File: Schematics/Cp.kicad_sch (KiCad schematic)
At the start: 56 parts, among them Q10 J201, Q11 J201, Q3 2SC1815, Q5 2SC1815, Q6 2SC1815, Q7 2SC1815, Q8 2SC1815, Q9 2SC1815, SW1 SW_DPDT_x2, U1 CA3080

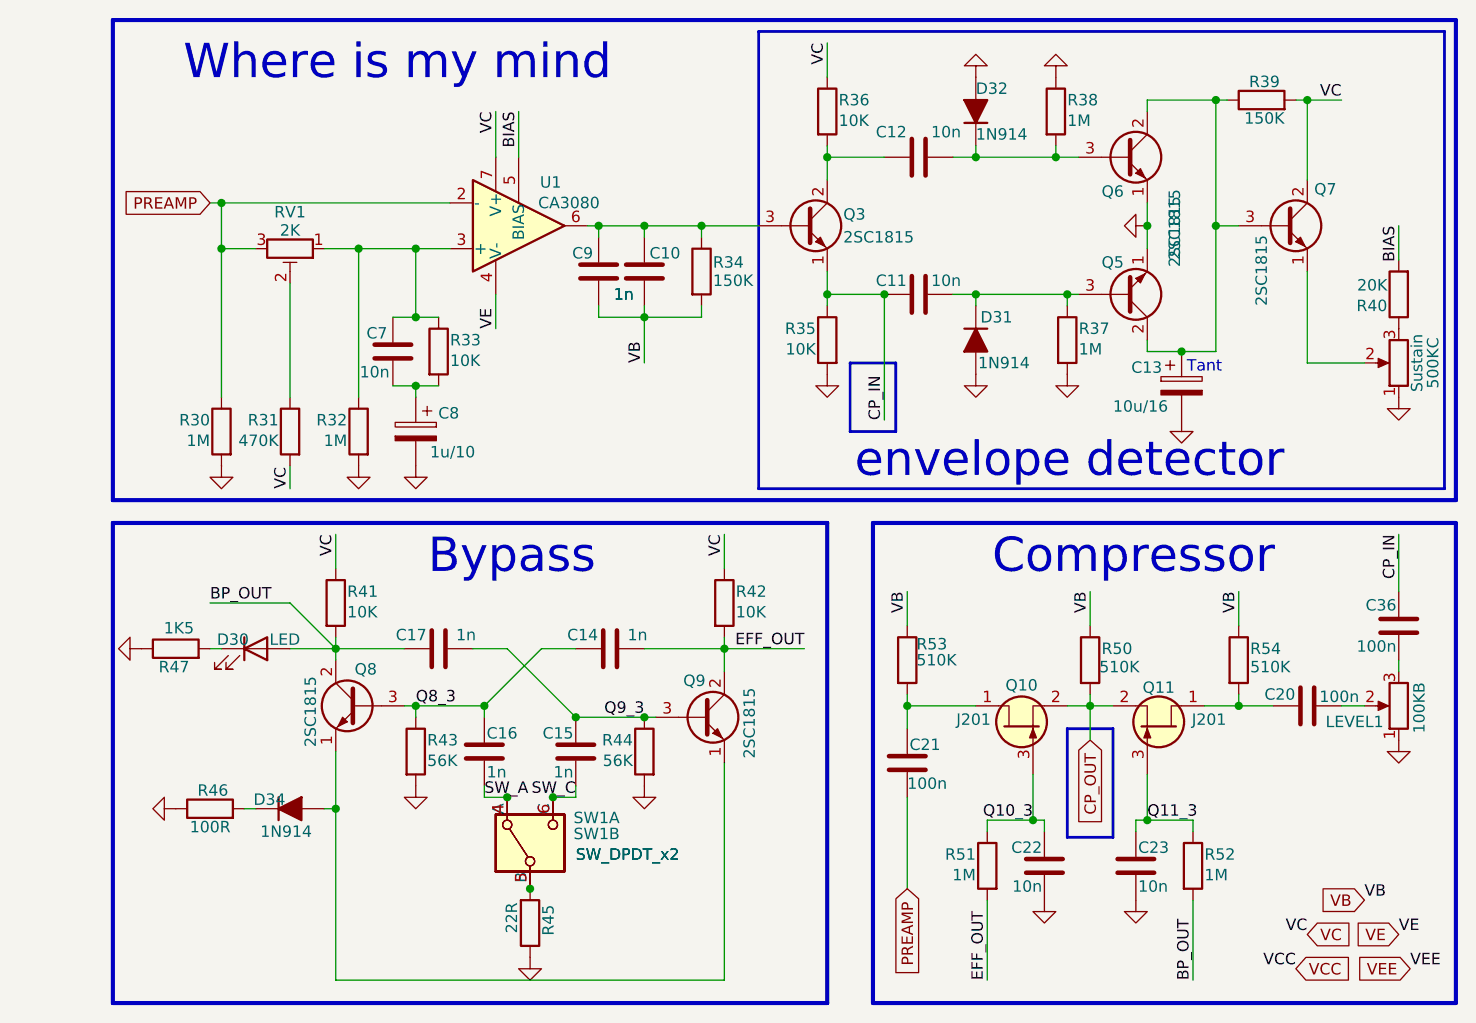
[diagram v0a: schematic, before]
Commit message: Schematic upd
Revorked bypass module, Annotated capacitors, Replaced 2N5484 and j209 with 2SK30A
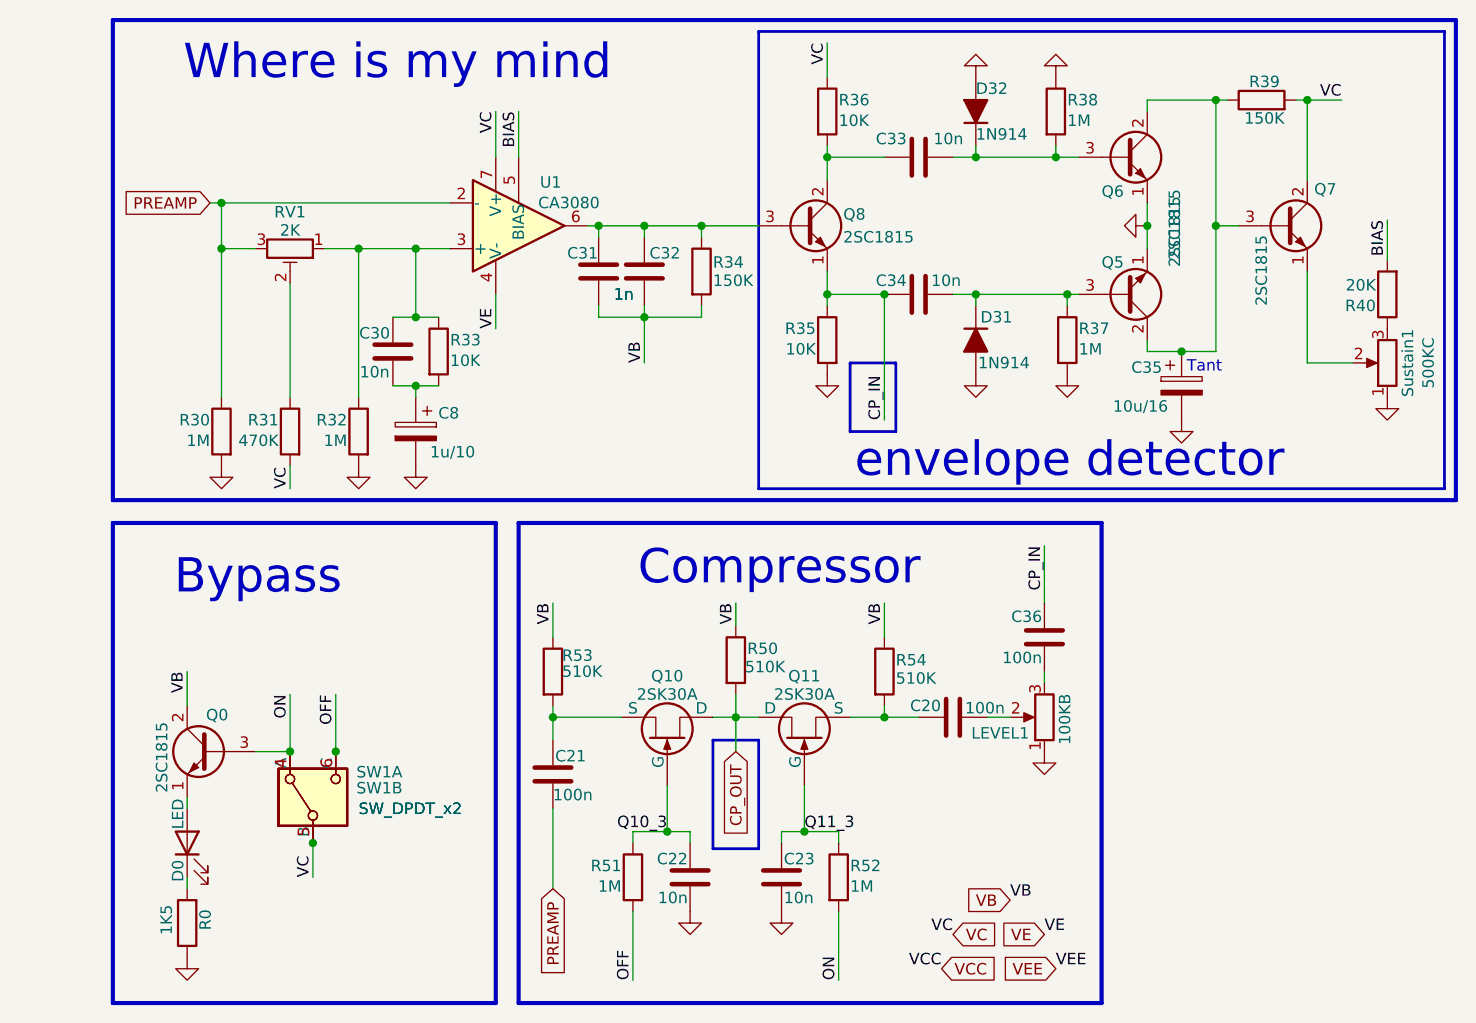
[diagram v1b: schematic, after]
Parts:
- removed C14, C15, C16, C17: 1n, PrLib:C_Disc_D4.3_W1.9_P5.00, symbol Device:C
- removed D30: LED, LED_THT:LED_D3.0mm_Horizontal_O6.35mm_Z6.0mm, symbol Device:LED
- removed D34: 1N914, Diode_THT:D_DO-35_SOD27_P7.62mm_Horizontal, symbol PCM_Diode_AKL:1N914
- removed Q10, Q11: J201, Package_TO_SOT_THT:TO-92_Inline, symbol PCM_Transistor_JFET_AKL:J201
- removed Q9: 2SC1815, Package_TO_SOT_THT:TO-92_Inline, symbol Transistor_BJT:2SC1815
- removed R41, R42: 10K, Resistor_THT:R_Axial_DIN0207_L6.3mm_D2.5mm_P10.16mm_Horizontal, symbol Device:R
- removed R43, R44: 56K, Resistor_THT:R_Axial_DIN0207_L6.3mm_D2.5mm_P10.16mm_Horizontal, symbol Device:R
- removed R45: 22R, Resistor_THT:R_Axial_DIN0207_L6.3mm_D2.5mm_P10.16mm_Horizontal, symbol Device:R
- removed R46: 100R, Resistor_THT:R_Axial_DIN0207_L6.3mm_D2.5mm_P10.16mm_Horizontal, symbol Device:R
- added D0: LED, LED_THT:LED_D3.0mm_Horizontal_O6.35mm_Z6.0mm, symbol Device:LED
- added Q10, Q11: 2SK30A, Package_TO_SOT_THT:TO-92_Inline_Wide, symbol Device:Q_NJFET_DGS
- renumbered C7 to C30, C9 to C31, C10 to C32, C12 to C33, C11 to C34, C13 to C35, Q8 to Q0, Q3 to Q8, R47 to R0, Sustain to Sustain1
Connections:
- net Q8_3 is gone; now on net ON: Q0.3 (B)
- net SW_A is gone; now on net ON: SW1.1 (A), SW1.4 (A)
- net SW_C is gone; now on net OFF: SW1.3 (C), SW1.6 (C)
- net CP_OUT: now also Q10.1 (D), Q11.1 (D)
- net Q10_3: now also Q10.2 (G)
- net Q11_3: now also Q11.2 (G)
- net VB: now also Q0.2 (C)
- net VC: now also SW1.2 (B), SW1.5 (B)
- net at C20.1, R54.2: now also Q11.3 (S)
- net at Q0.1 (E): now also D0.2 (A)
- net at C21.2, R53.2: now also Q10.3 (S)
- net at R0.2: now also D0.1 (K)
- net BP_OUT renamed ON
- net ON: no longer Q0.2 (C)
- net EFF_OUT renamed OFF
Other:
- moved on the sheet: C20, C21, C22, C23, C36, LEVEL1, Q0, R0, R40, R50, R51, R52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

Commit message: Schematic upd
Revorked mix module, Bypass upd, Replaced 1N914 with 1N4148
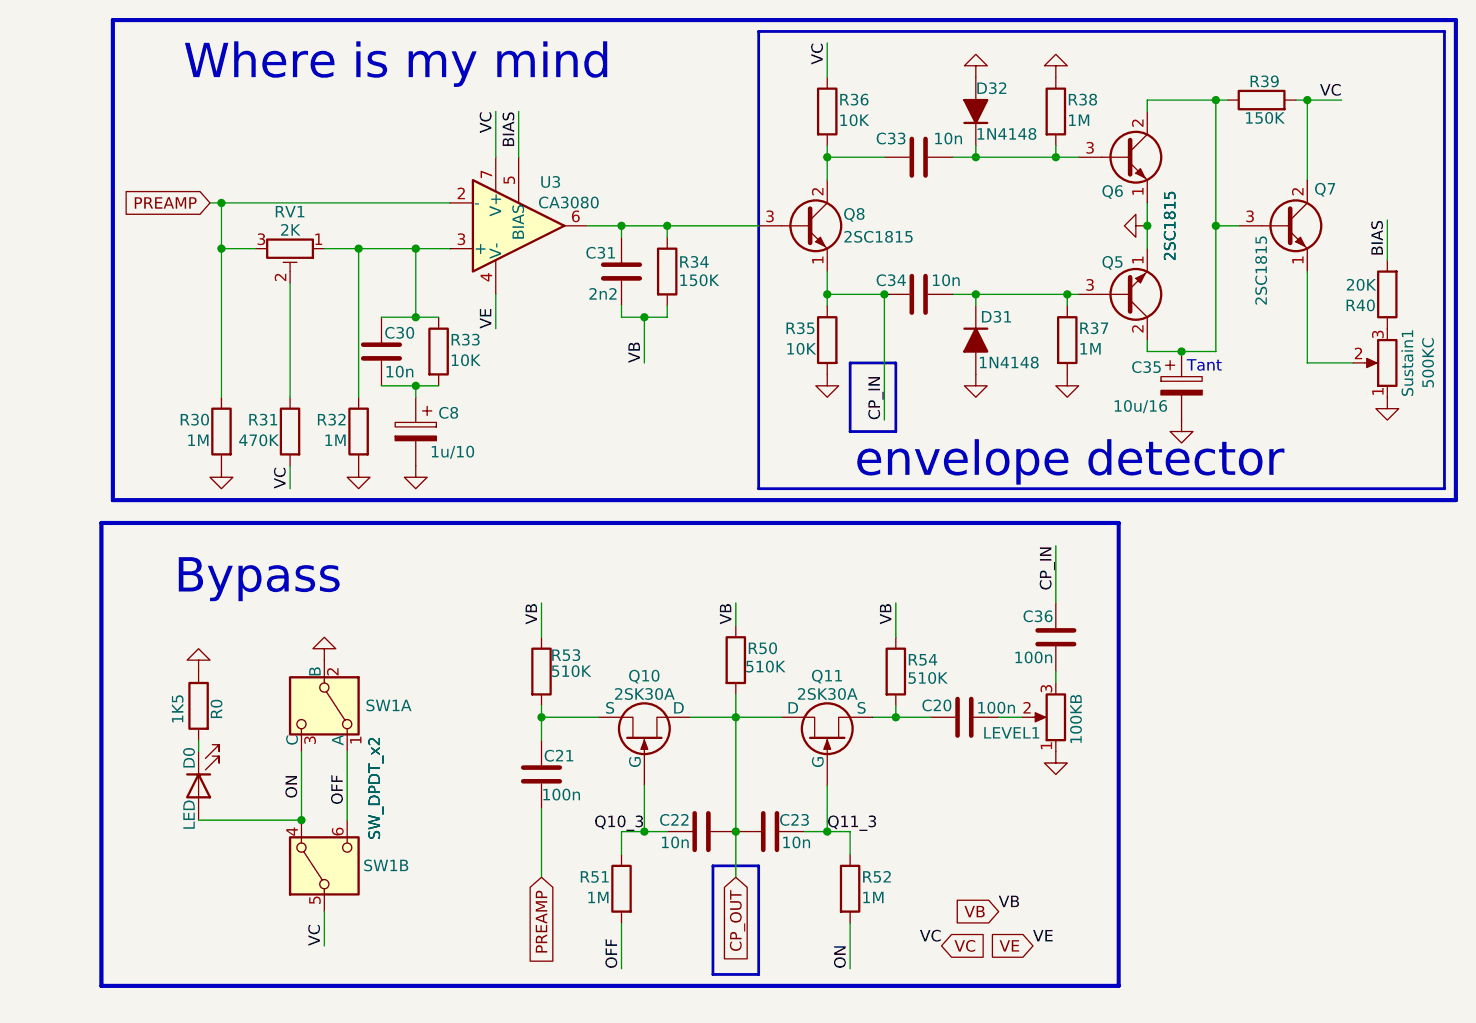
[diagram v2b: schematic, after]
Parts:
- removed C32: 1n, PrLib:C_Disc_D4.3_W1.9_P5.00, symbol Device:C
- removed Q0: 2SC1815, Package_TO_SOT_THT:TO-92_Inline, symbol Transistor_BJT:2SC1815
- C31: value 1n -> 2n2
- D31, D32: value 1N914 -> 1N4148
- renumbered U1 to U3
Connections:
- net VС is gone; now on net VC: U3.7 (V+)
- net CP_OUT: now also C22.1, C23.2
- net GND: now also SW1.2 (B); no longer C22.1, C23.1
- net OFF: now also SW1.1 (A); no longer SW1.3 (C)
- net ON: now also D0.2 (A), SW1.3 (C); no longer SW1.1 (A)
- net Q11_3: now also C23.1; no longer C23.2
- net VC: no longer SW1.2 (B)
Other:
- note removed: "Compressor"
- moved on the sheet: C20, C21, C22, C23, C30, C31, C36, D0, LEVEL1, Q10, Q11, R0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
